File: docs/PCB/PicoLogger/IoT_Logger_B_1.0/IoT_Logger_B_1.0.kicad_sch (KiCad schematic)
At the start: 31 parts, among them J1 JTAG, U1 STM32F412RGTx, Y1 3225-25M-SR, Y2 32.768K-CFPX217

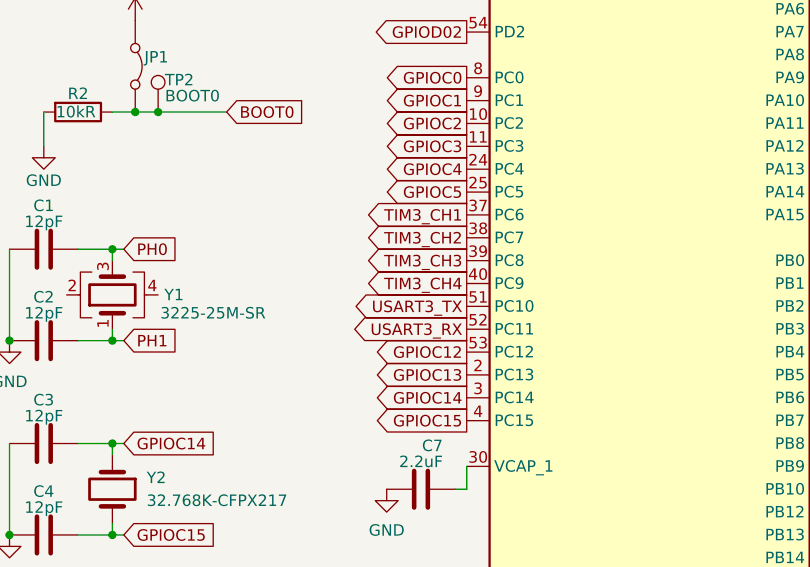
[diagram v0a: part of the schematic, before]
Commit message: HAL and LL prototypes added.
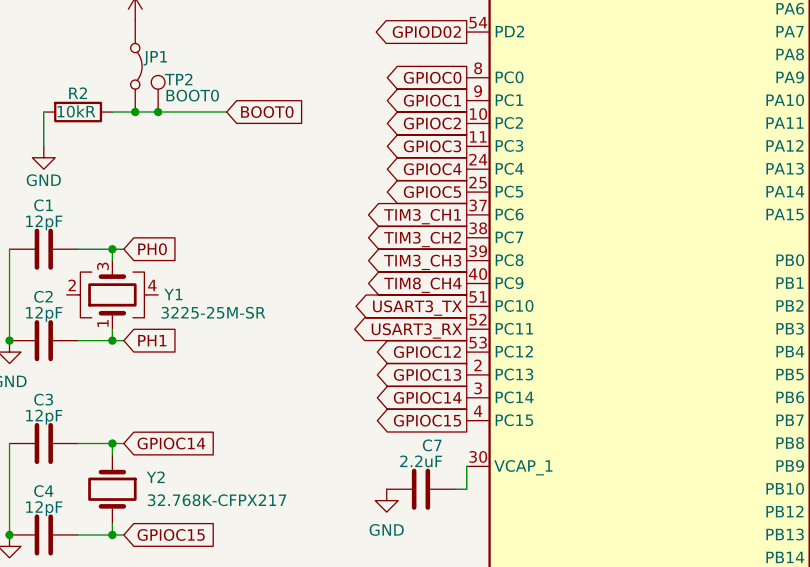
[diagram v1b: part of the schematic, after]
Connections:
- net TIM3_CH4 renamed TIM8_CH4
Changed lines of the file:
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@@
 		)
 	)
-	(global_label "TIM3_CH4"
+	(global_label "TIM8_CH4"
 		(shape output)
 		(at 130.81 120.65 180)
